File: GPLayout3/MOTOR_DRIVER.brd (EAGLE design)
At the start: 91.4 x 97.5 mm, 91 parts, among them T1 2N2222, T2 2N2222, U7 ATMEGA328P_TQFP, Y1 16MHz

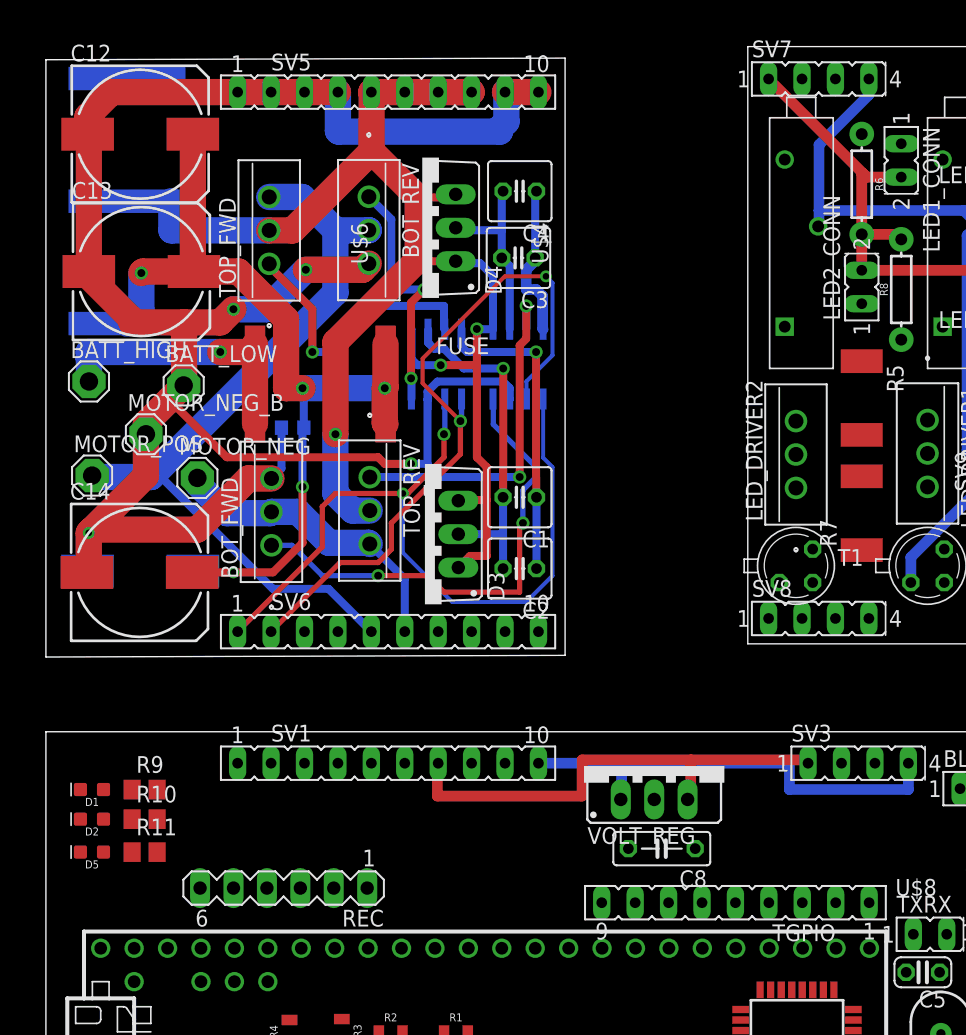
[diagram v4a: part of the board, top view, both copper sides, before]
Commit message: Added current sense, needed to change a few pins on upper left. Check routing again. Changed rec header to female
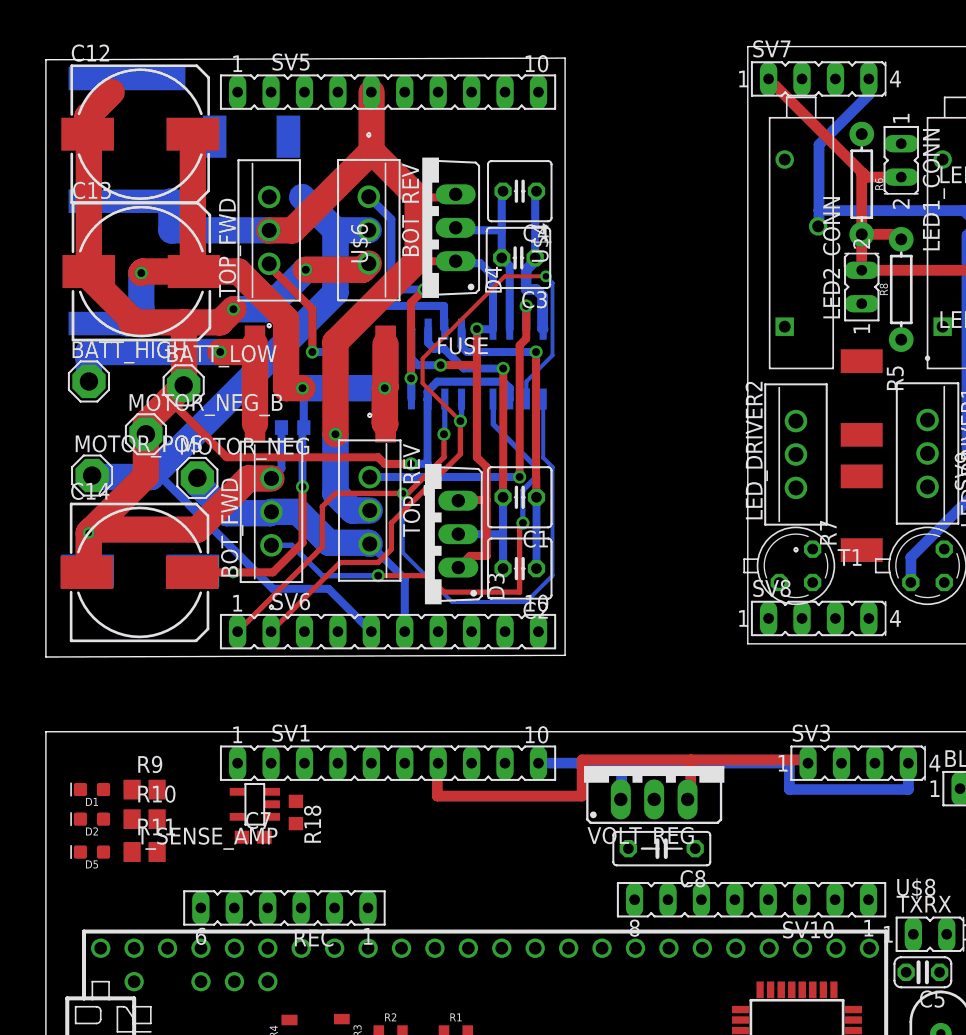
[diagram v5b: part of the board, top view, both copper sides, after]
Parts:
- removed TGPIO: (no value), con-lsta:FE09
- added C7: (no value), resistor:C0603
- added I_SENSE_AMP: INA138, burr-brown:SOT23-5
- added R17: 10m, rcl:R2512
- added R18: 10k, rcl:R0603
- added SV10: (no value), con-lsta:FE08
- REC: device con-lstb:MA06-1 -> con-lsta:FE06
- moved REC 1.51 mm to (18.1, 32.0)
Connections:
- removed net HI2_TOP: SV6.3
- removed net LI2_TOP: SV6.4
- removed net TGPIO9: TGPIO.9, U$1.A22/DAC1
- new net 7_4_TOP: SV5.3, SV5.4, SV5.5, SV5.6
- new net I_SENSE: I_SENSE_AMP.1, R18.2, U$1.A22/DAC1
- new net I_SENSE_HI: I_SENSE_AMP.3, SV1.2
- new net I_SENSE_HI_TOP: BOT_REV.2, R17.1, SV5.2, TOP_FWD.3
- new net I_SENSE_LOW: I_SENSE_AMP.4, SV1.1
- new net I_SENSE_LOW_TOP: MOTOR_POS.MP, R17.2, SV5.1
- net 7_4V: now also C7.1, I_SENSE_AMP.5, SV1.3, SV1.4, SV1.5, SV1.6; no longer SV1.7
- net 7_4V_TOP: no longer SV5.5, SV5.6, SV5.7, SV5.8
- net GND: now also C7.2, I_SENSE_AMP.2, R18.1, SV1.7, SV1.8, SV1.9
- net GND_TOP: now also SV5.7, SV5.8; no longer SV5.1, SV5.2, SV5.3, SV5.4
- net MOTOR_HIGH_TOP: no longer BOT_REV.2, MOTOR_POS.MP, TOP_FWD.3
- net TGPIO1: now also SV10.1; no longer TGPIO.1
- net TGPIO2: now also SV10.2; no longer TGPIO.2
- net TGPIO3: now also SV10.3; no longer TGPIO.3
- net TGPIO4: now also SV10.4; no longer TGPIO.4
- net TGPIO5: now also SV10.5; no longer TGPIO.5
- net TGPIO6: now also SV10.6; no longer TGPIO.6
- net TGPIO7: now also SV10.7; no longer TGPIO.7
- net TGPIO8: now also SV10.8; no longer TGPIO.8
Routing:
- net GND_TOP: track 160.3 -> 122.1 mm
- net 7_4V_TOP: track 114.3 -> 105.5 mm
- net MOTOR_HIGH_TOP: track 59.3 -> 56.6 mm

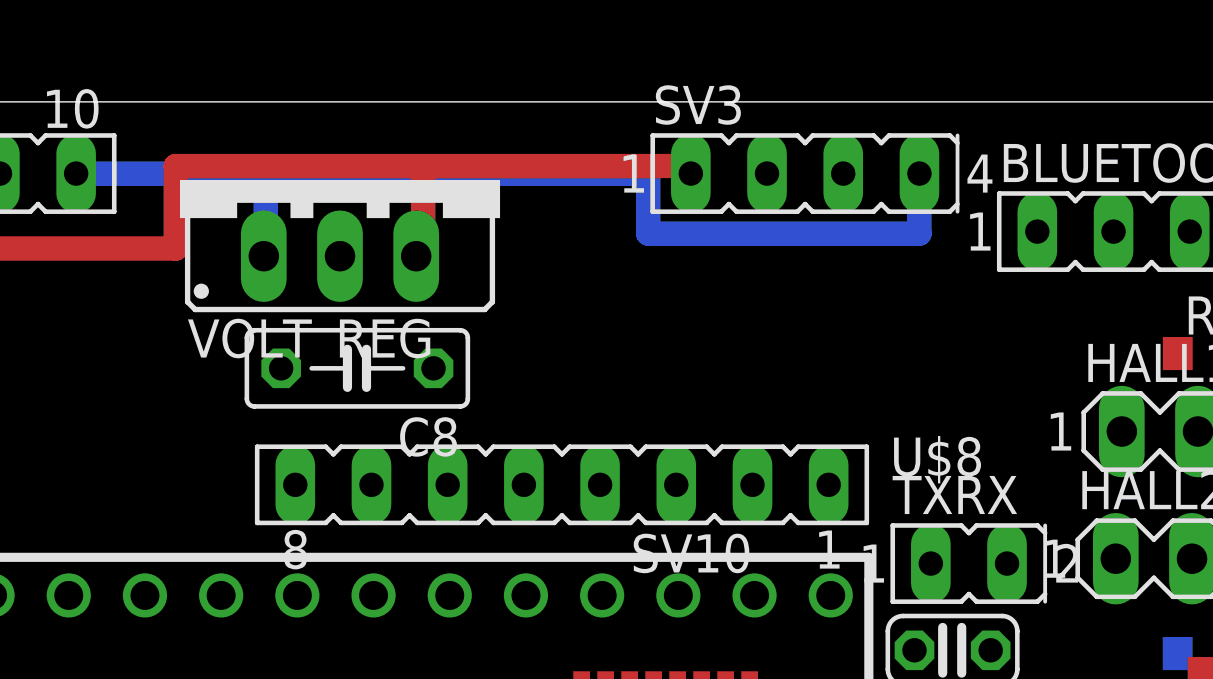
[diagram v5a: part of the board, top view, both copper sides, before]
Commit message: changed voltage regulator cap
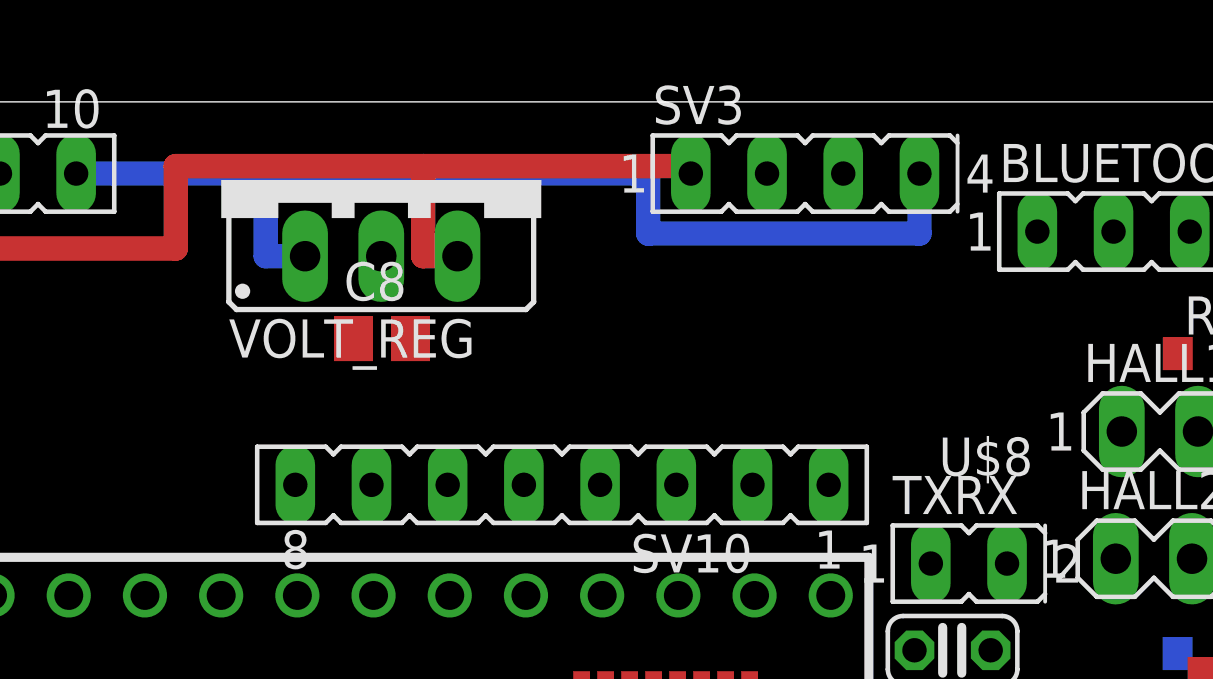
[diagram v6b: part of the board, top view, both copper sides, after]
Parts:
- C8: value 10uF -> 10u; device resistor:C050-025X075 -> rcl:C0805
- moved U$8 1.62 mm to (47.6, 44.0)
- moved VOLT_REG 1.38 mm to (47.6, 42.8)
- moved C8 1.29 mm to (47.6, 37.5), turned to 0 degrees
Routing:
- net GND: track 34.9 -> 36.2 mm
- net 7_4V: track 36.9 -> 37.8 mm
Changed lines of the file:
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@@
 <element name="BATT_HIGH" library="solpad" package="SE14" value="SE14" x="3.27" y="72.01"/>
 <element name="BATT_LOW" library="solpad" package="SE14" value="SE14" x="10.47" y="71.71"/>
-<element name="C8" library="resistor" package="C050-025X075" value="10uF" x="46.804" y="36.508" rot="R180"/>
 <element name="C12" library="resistor" package="153CLV-1010" value="33u" x="7.166" y="90.8"/>
 <element name="C13" library="resistor" package="153CLV-1010" value="33u" x="7.258" y="80.362"/>
@@
 <attribute name="DIGIKEY_PART_NUMBER" value="HS112-ND" x="13.394" y="62.364" size="1.778" layer="27" rot="R270" display="off"/>
 </element>
-<element name="VOLT_REG" library="v-reg-3" package="TO220S" value="LM1086TO220V" x="46.226" y="42.786">
-<attribute name="DIGIKEY_PART_NUMBER" value="LM1086IT-5.0/NOPB-ND" x="46.226" y="42.786" size="1.778" layer="27" display="off"/>
-<attribute name="MANUFACTURER" value="Texas Instruments" x="46.226" y="42.786" size="1.778" layer="27" display="off"/>
-<attribute name="MANUFACTURER_PART_NUMBER" value="LM1086IT-5.0/NOPB" x="46.226" y="42.786" size="1.778" layer="27" display="off"/>
-<attribute name="PRICE" value="$1.67" x="46.226" y="42.786" size="1.778" layer="27" display="off"/>
+<element name="VOLT_REG" library="v-reg-3" package="TO220S" value="LM1086TO220V" x="47.601" y="42.786">
+<attribute name="DIGIKEY_PART_NUMBER" value="LM1086IT-5.0/NOPB-ND" x="47.601" y="42.786" size="1.778" layer="27" display="off"/>
+<attribute name="MANUFACTURER" value="Texas Instruments" x="47.601" y="42.786" size="1.778" layer="27" display="off"/>
+<attribute name="MANUFACTURER_PART_NUMBER" value="LM1086IT-5.0/NOPB" x="47.601" y="42.786" size="1.778" layer="27" display="off"/>
+<attribute name="PRICE" value="$1.67" x="47.601" y="42.786" size="1.778" layer="27" display="off"/>
 </element>
 <element name="CAMERA" library="con-lsta" package="FE05-1" value="" x="78.222" y="9.45">
@@
 <element name="LED2_CONN" library="con-lsta" package="FE02-1" value="" x="62" y="83" rot="R90"/>
 <element name="SV9" library="con-lsta" package="FE02-1" value="" x="72" y="70" rot="R90"/>
-<element name="U$8" library="heatsink" package="HEATSINK" value="" x="46" y="44" rot="R180"/>
+<element name="U$8" library="heatsink" package="HEATSINK" value="" x="47.625" y="44" rot="R180"/>
 <element name="GROUND" library="con-lsta" package="FE05-1" value="" x="88" y="8" rot="R90"/>
 <element name="3_3V" library="con-lsta" package="FE05-1" value="" x="78" y="3"/>
@@
 <attribute name="OC_FARNELL" value="unknown" x="18.125" y="32" size="1.778" layer="27" rot="R180" display="off"/>
 </element>
+<element name="C8" library="rcl" package="C0805" value="10u" x="47.625" y="37.5"/>
 </elements>
 <signals>
@@
 <contactref element="R2" pad="1"/>
 <contactref element="SV1" pad="10"/>
-<contactref element="C8" pad="2"/>
 <contactref element="VOLT_REG" pad="1"/>
 <contactref element="CAMERA" pad="1"/>
@@
 <wire x1="56.5" y1="41" x2="65.54" y2="41" width="0.8128" layer="16"/>
 <wire x1="65.54" y1="41" x2="65.54" y2="43" width="0.8128" layer="16"/>
-<wire x1="43.686" y1="40.246" x2="43.75" y2="40.246" width="0.8128" layer="16"/>
+<wire x1="45.061" y1="40.246" x2="43.75" y2="40.246" width="0.8128" layer="16"/>
 <wire x1="43.75" y1="40.246" x2="43.75" y2="43" width="0.8128" layer="16"/>
 <contactref element="SV1" pad="9"/>
@@
 <contactref element="C7" pad="2"/>
 <contactref element="REC" pad="1"/>
+<contactref element="C8" pad="2"/>
 <wire x1="83.126" y1="34.422" x2="85.698" y2="39.726" width="0" layer="19" extent="1-1"/>
 <wire x1="83.126" y1="30.082" x2="83.126" y2="34.422" width="0" layer="19" extent="1-1"/>
@@
 <wire x1="32.35" y1="43" x2="34.89" y2="43" width="0" layer="19" extent="1-1"/>
 <wire x1="29.81" y1="43" x2="32.35" y2="43" width="0" layer="19" extent="1-1"/>
-<wire x1="44.264" y1="36.508" x2="43.686" y2="40.246" width="0" layer="19" extent="1-1"/>
-<wire x1="39.724" y1="28.938" x2="44.264" y2="36.508" width="0" layer="19" extent="1-1"/>
 <wire x1="65.375" y1="27.11" x2="74.626" y2="30.162" width="0" layer="19" extent="1-1"/>
 <wire x1="61.3706" y1="21.882" x2="65.375" y2="27.11" width="0" layer="19" extent="1-1"/>
@@
 <wire x1="17.181" y1="39.875" x2="19" y2="40.1" width="0" layer="19" extent="1-1"/>
 <wire x1="16.6" y1="37.375" x2="17.181" y2="39.875" width="0" layer="19" extent="1-1"/>
+<wire x1="24.475" y1="32" x2="16.6" y2="37.375" width="0" layer="19" extent="1-1"/>
+<wire x1="25.302" y1="22.49" x2="24.475" y2="32" width="0" layer="19" extent="1-1"/>
+<wire x1="39.724" y1="28.938" x2="43.75" y2="40.246" width="0" layer="19" extent="16-16"/>
 <wire x1="6.704" y1="28.938" x2="16.6" y2="37.375" width="0" layer="19" extent="1-1"/>
 <wire x1="2.623" y1="36.25" x2="6.704" y2="28.938" width="0" layer="19" extent="1-1"/>
@@
 <wire x1="2.623" y1="41" x2="2.623" y2="38.75" width="0" layer="19" extent="1-1"/>
 <wire x1="4.164" y1="13.698" x2="6.704" y2="28.938" width="0" layer="19" extent="1-1"/>
-<wire x1="25.302" y1="22.49" x2="39.724" y2="28.938" width="0" layer="19" extent="1-1"/>
-<wire x1="24.475" y1="32" x2="4.164" y2="13.698" width="0" layer="19" extent="1-1"/>
+<wire x1="48.575" y1="37.5" x2="4.164" y2="13.698" width="0" layer="19" extent="1-1"/>
 </signal>
 <signal name="N$6">
@@
 <contactref element="S1" pad="7"/>
 <contactref element="VOLT_REG" pad="2"/>
-<contactref element="C8" pad="1"/>
 <contactref element="SERVO" pad="2"/>
 <contactref element="5V" pad="5"/>
@@
 <contactref element="5V" pad="1"/>
 <contactref element="REC" pad="2"/>
+<contactref element="C8" pad="1"/>
 <wire x1="84.4758" y1="13.64" x2="83.158" y2="39.726" width="0" layer="19" extent="1-1"/>
 <wire x1="83.08" y1="6" x2="84.4758" y2="13.64" width="0" layer="19" extent="1-1"/>
@@
 <wire x1="75.46" y1="6" x2="78" y2="6" width="0" layer="19" extent="1-1"/>
 <wire x1="72.92" y1="6" x2="75.46" y2="6" width="0" layer="19" extent="1-1"/>
-<wire x1="49.344" y1="36.508" x2="83.158" y2="39.726" width="0" layer="19" extent="1-1"/>
-<wire x1="46.226" y1="40.246" x2="49.344" y2="36.508" width="0" layer="19" extent="1-1"/>
-<wire x1="21.935" y1="32" x2="49.344" y2="36.508" width="0" layer="19" extent="1-1"/>
+<wire x1="47.601" y1="40.246" x2="83.158" y2="39.726" width="0" layer="19" extent="1-1"/>
+<wire x1="21.935" y1="32" x2="47.601" y2="40.246" width="0" layer="19" extent="1-1"/>
+<wire x1="46.675" y1="37.5" x2="21.935" y2="32" width="0" layer="19" extent="1-1"/>
 </signal>
 <signal name="3_3V">
@@
 <wire x1="49" y1="43.25" x2="57.92" y2="43.25" width="0.8128" layer="1"/>
 <wire x1="57.92" y1="43.25" x2="57.92" y2="43" width="0.8128" layer="1"/>
-<wire x1="48.766" y1="40.246" x2="49" y2="40.246" width="0.8128" layer="1"/>
+<wire x1="50.141" y1="40.246" x2="49" y2="40.246" width="0.8128" layer="1"/>
 <wire x1="49" y1="40.246" x2="49" y2="43.25" width="0.8128" layer="1"/>
 <contactref element="SV1" pad="6"/>

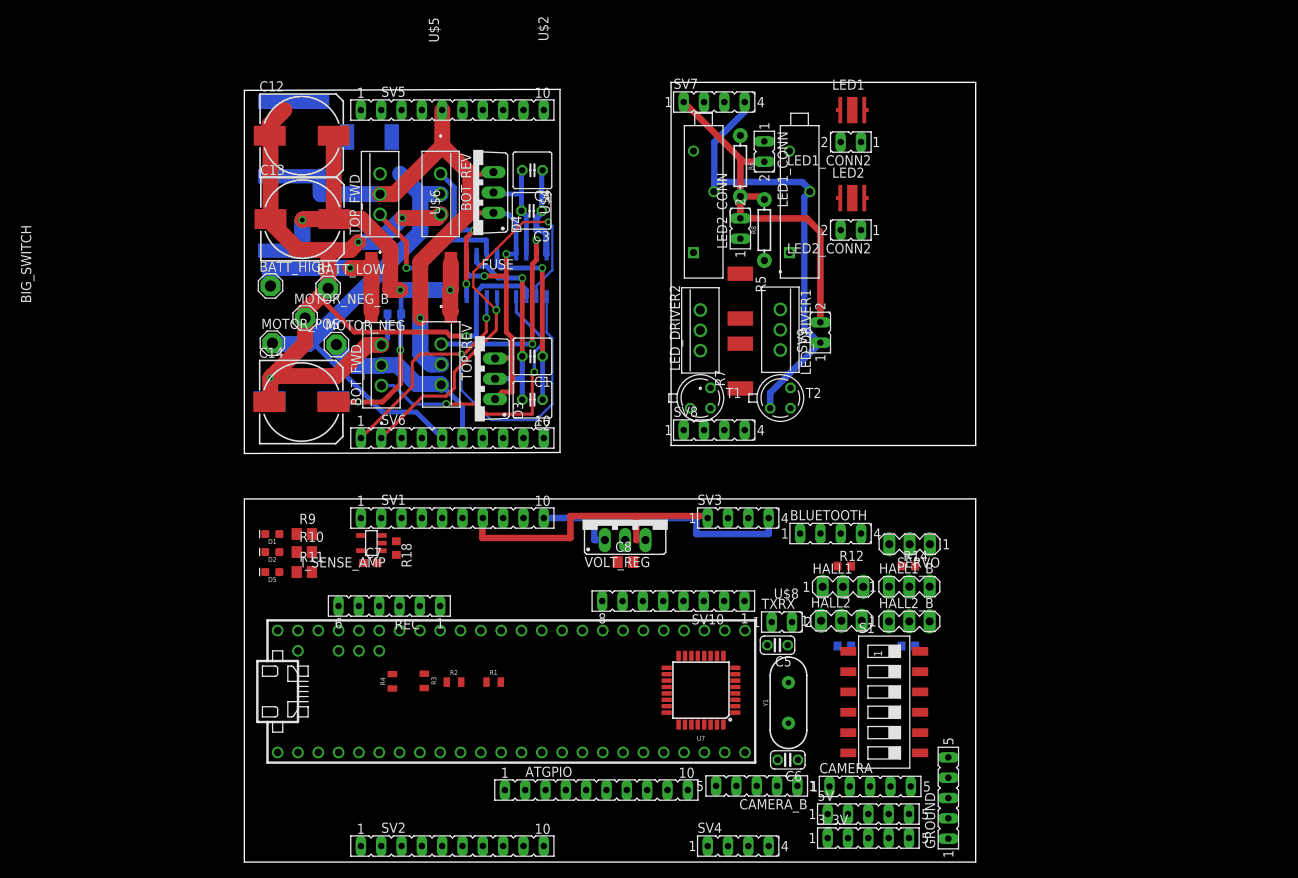
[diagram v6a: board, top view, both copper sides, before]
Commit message: Updated top routing to include current sense resistor at 135 degree angle.
4pcb should be checked to see if they can make the pads for the angled
component
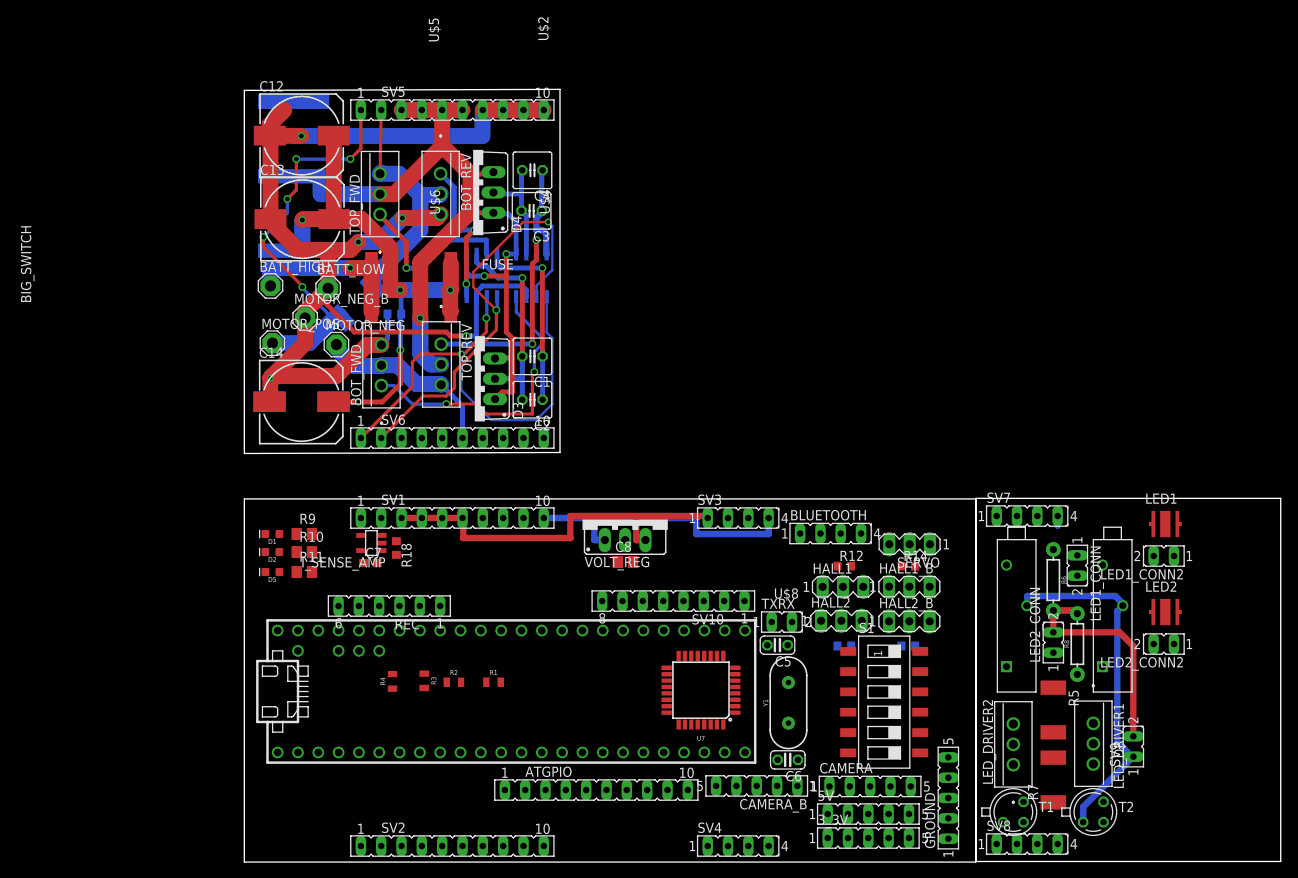
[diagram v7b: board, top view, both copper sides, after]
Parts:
- moved LED1 64.9 mm to (115.1, 42.2)
- moved LED1_CONN 64.9 mm to (104.1, 33.2)
- moved LED1_CONN2 64.9 mm to (111.1, 38.2)
- moved LED2 64.9 mm to (115.1, 31.2)
- moved LED2_CONN 64.9 mm to (101.1, 31.2)
- moved LED2_CONN2 64.9 mm to (111.1, 27.2)
- moved LED_DRIVER1 64.9 mm to (106.1, 12.2)
- moved LED_DRIVER2 64.9 mm to (96.1, 17.2)
- moved R5 64.9 mm to (101.1, 19.0)
- moved R6 64.9 mm to (101.1, 35.2)
- moved R7 64.9 mm to (101.1, 10.2)
- moved R8 64.9 mm to (104.1, 27.2)
- moved SV7 64.9 mm to (99.1, 43.2)
- moved SV8 64.9 mm to (99.1, 2.25)
- moved SV9 64.9 mm to (111.1, 18.2)
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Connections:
- removed net 7_4_TOP: SV5.3, SV5.4, SV5.5, SV5.6
- net 7_4V_TOP: now also SV5.3, SV5.4, SV5.5, SV5.6
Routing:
- net MOTOR_HIGH_TOP: track 56.6 -> 0.00 mm
- net I_SENSE_LOW_TOP: track 0.00 -> 49.3 mm, vias 0 -> 5
- net GND_TOP: track 122.1 -> 159.5 mm, vias 4 -> 5
- net I_SENSE_HI_TOP: track 0.00 -> 30.7 mm
- net 7_4V_TOP2: track 45.7 -> 27.9 mm
- net GND_TOP2: track 56.3 -> 45.9 mm
- net 7_4V: track 37.8 -> 47.9 mm
- net 7_4V_TOP: track 105.5 -> 113.1 mm
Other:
- board size 91.4 x 97.5 mm -> 129.5 x 96.6 mm
